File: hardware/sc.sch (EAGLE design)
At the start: 99 parts, among them IC1 PB137ACV, IC2 INA168, Q1 si2305cd, Q2 8MHz 18pF, Q3 IRFR5305, T1 BC846, U1 SPX5205 3v3, U6 microSD Socket, X3 MKDSN1,5/4-5,08, Y1 32768Hz CFPX-217 12.5pF

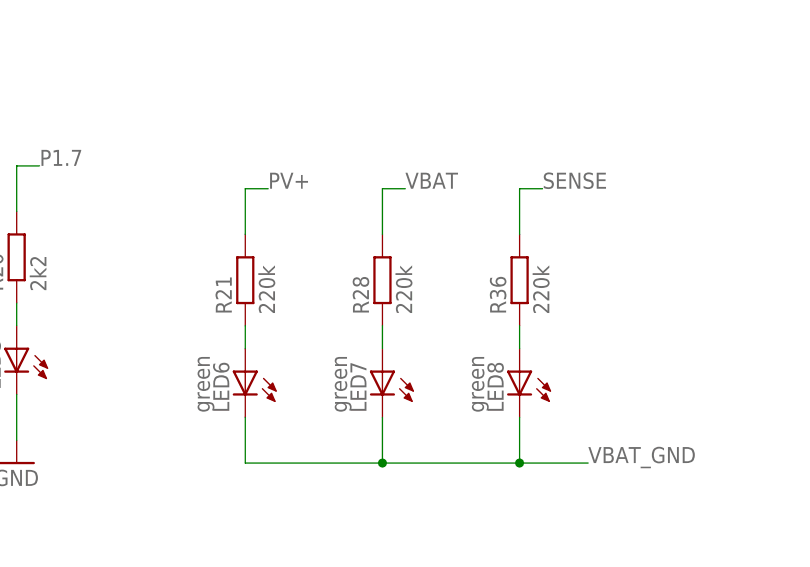
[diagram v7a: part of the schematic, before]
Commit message: keep track of programming time
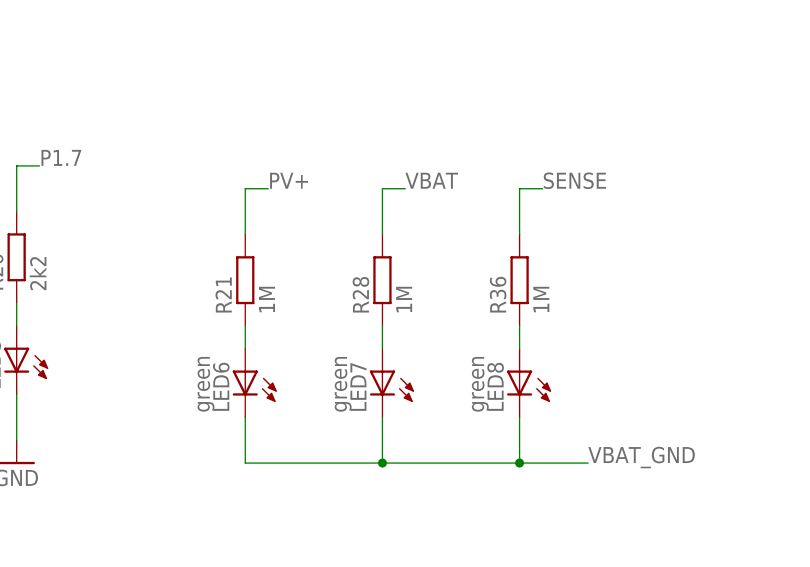
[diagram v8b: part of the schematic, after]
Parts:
- R21, R28, R36: value 220k -> 1M
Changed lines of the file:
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@@
 <part name="LED5" library="led" deviceset="LED" device="CHIP-LED0805" value="green"/>
 <part name="GND48" library="SparkFun" deviceset="GND" device=""/>
-<part name="R21" library="rcl" deviceset="R-EU_" device="R0805W" value="220k"/>
+<part name="R21" library="rcl" deviceset="R-EU_" device="R0805W" value="1M"/>
 <part name="LED6" library="led" deviceset="LED" device="CHIP-LED0805" value="green"/>
-<part name="R28" library="rcl" deviceset="R-EU_" device="R0805W" value="220k"/>
+<part name="R28" library="rcl" deviceset="R-EU_" device="R0805W" value="1M"/>
 <part name="LED7" library="led" deviceset="LED" device="CHIP-LED0805" value="green"/>
-<part name="R36" library="rcl" deviceset="R-EU_" device="R0805W" value="220k"/>
+<part name="R36" library="rcl" deviceset="R-EU_" device="R0805W" value="1M"/>
 <part name="LED8" library="led" deviceset="LED" device="CHIP-LED0805" value="green"/>
 <part name="D2" library="diode" deviceset="DIODE-" device="C1702-05" value="SB560"/>
